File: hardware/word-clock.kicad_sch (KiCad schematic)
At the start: 51 parts, among them SW1 Hour, SW2 Minute, SW3 Audio, U1 ESP32 CP2102, U2 74HC245

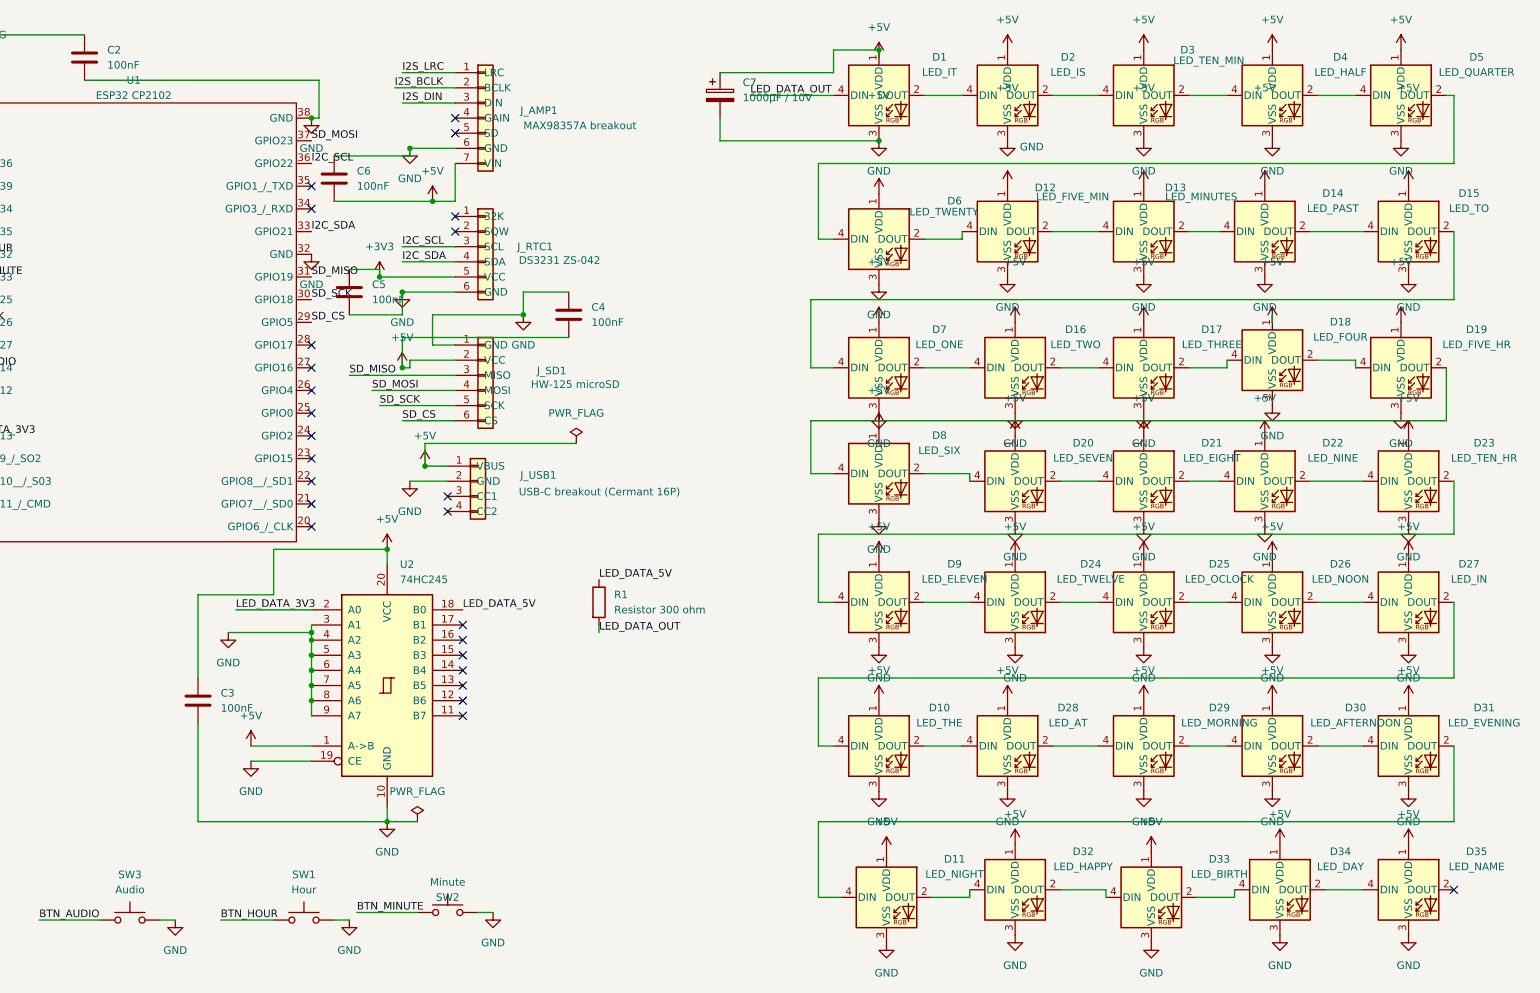
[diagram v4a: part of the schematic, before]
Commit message: feat(hardware): led chain reorder, AT relocated, routing + pour complete
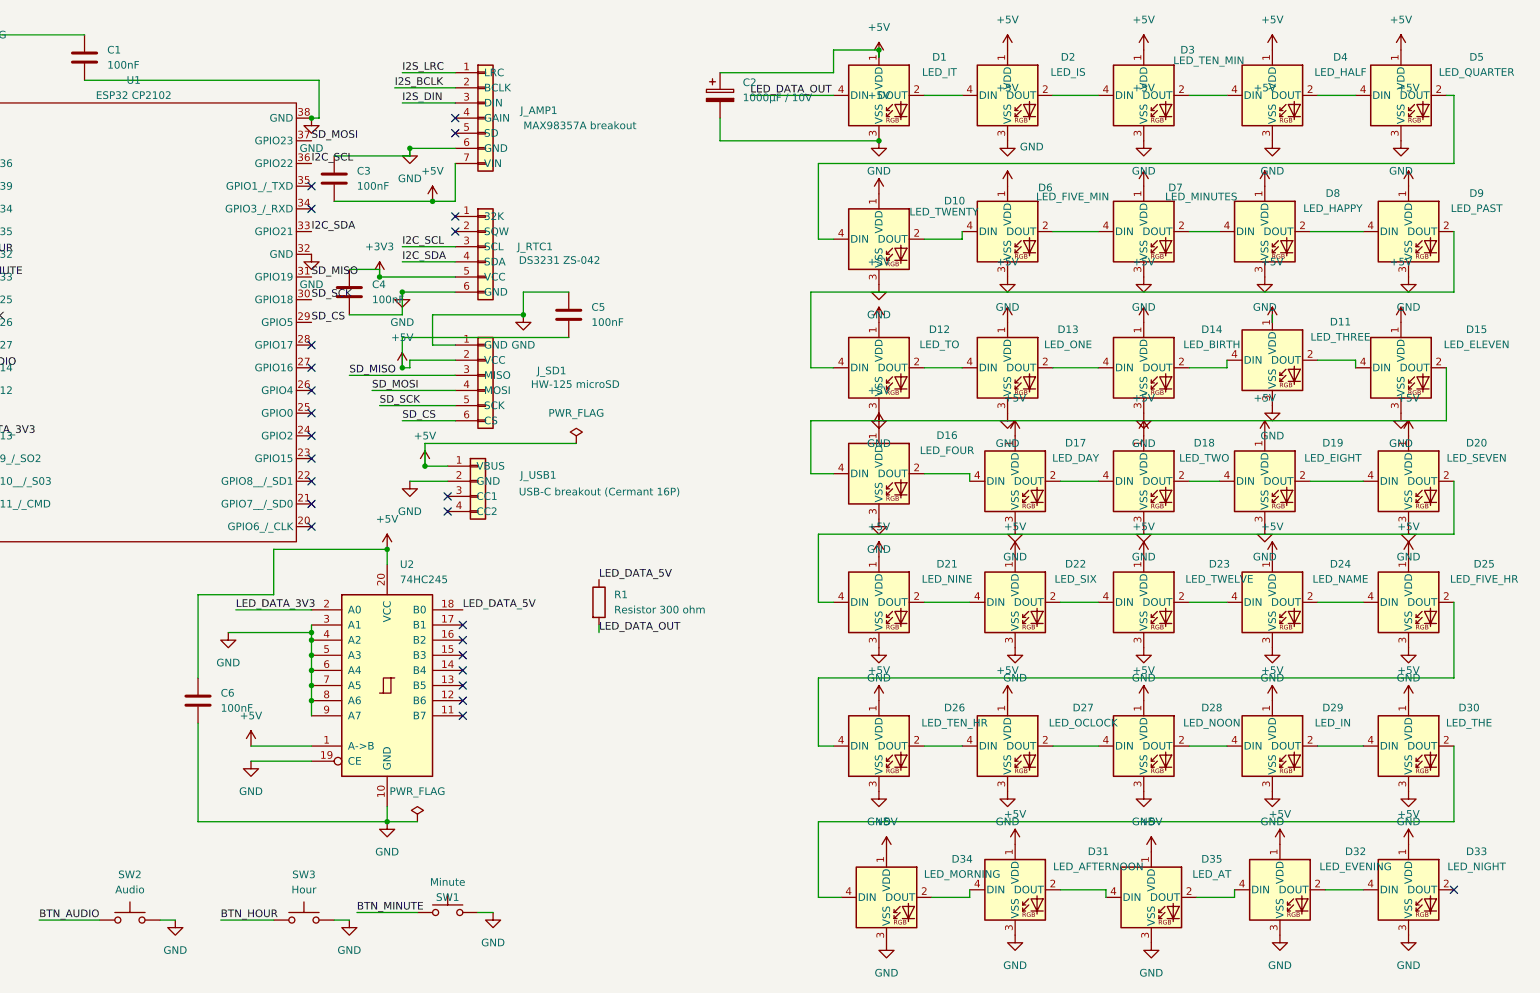
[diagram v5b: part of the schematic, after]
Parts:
- renumbered C2 to C1, C7 to C2, C6 to C3, C5 to C4, C4 to C5, C3 to C6, D6 to D10, D17 to D11, D15 to D12, D7 to D13, D33 to D14, D9 to D15, D18 to D16, D34 to D17, D16 to D18, D21 to D19, D22 to D21, D8 to D22, D24 to D23, D35 to D24, D19 to D25, D23 to D26, D25 to D27, D26 to D28, D27 to D29, D10 to D30, D30 to D31, D31 to D32, D11 to D33, D29 to D34, D28 to D35, D12 to D6, D13 to D7, D32 to D8, D14 to D9, SW2 to SW1, SW3 to SW2, SW1 to SW3
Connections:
- net at D25.2 (DOUT): now also D26.4 (DIN); no longer D22.4 (DIN)
- net at D25.4 (DIN): now also D24.2 (DOUT); no longer D16.2 (DOUT)
- net at D7.2 (DOUT): now also D8.4 (DIN); no longer D9.4 (DIN)
- net at D23.2 (DOUT): now also D24.4 (DIN); no longer D27.4 (DIN)
- net at D23.4 (DIN): now also D22.2 (DOUT); no longer D15.2 (DOUT)
- net at D11.2 (DOUT): now also D15.4 (DIN); no longer D16.4 (DIN)
- net at D11.4 (DIN): now also D14.2 (DOUT); no longer D18.2 (DOUT)
- net at D17.2 (DOUT): now also D18.4 (DIN); no longer D24.4 (DIN)
- net at D17.4 (DIN): now also D16.2 (DOUT); no longer D14.2 (DOUT)
- net at D31.2 (DOUT): now also D35.4 (DIN); no longer D32.4 (DIN)
- net at D33.2 (DOUT): no longer D8.4 (DIN)
- net at D26.2 (DOUT): now also D27.4 (DIN); no longer D15.4 (DIN)
- net at D21.2 (DOUT): now also D22.4 (DIN); no longer D26.4 (DIN)
- net at D30.2 (DOUT): now also D34.4 (DIN); no longer D35.4 (DIN)
- net at D21.4 (DIN): now also D20.2 (DOUT); no longer D19.2 (DOUT)
- net at D35.2 (DOUT): now also D32.4 (DIN); no longer D34.4 (DIN)
- net at D19.4 (DIN): now also D18.2 (DOUT); no longer D20.2 (DOUT)
- net at D20.4 (DIN): now also D19.2 (DOUT); no longer D22.2 (DOUT)
- net at D13.2 (DOUT): now also D14.4 (DIN); no longer D18.4 (DIN)
- net at D8.2 (DOUT): now also D9.4 (DIN); no longer D14.4 (DIN)
- new net: D15.2 (DOUT), D16.4 (DIN)
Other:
- moved on the sheet: D11, D12, D13, D14, D15, D16, D17, D18, D19, D20, D21, D22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

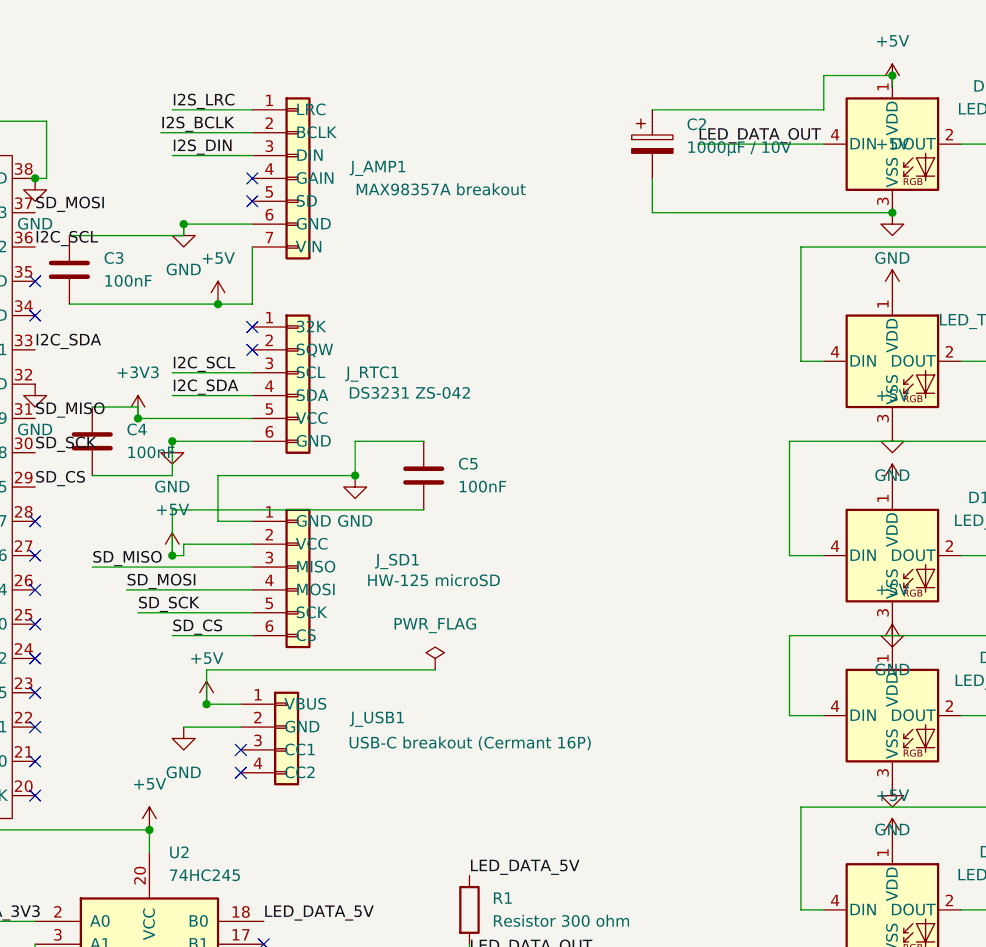
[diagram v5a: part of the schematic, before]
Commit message: fix(hardware): remove cermant usb-c breakout, power via esp32 micro-usb
Removes J_USB1 from the schematic and PCB. The user-facing USB-C port on
the back panel will now be provided by a panel-mount USB-C-female-to-
micro-USB-male pigtail plugged directly into the ESP32 module's native
micro-USB connector. The CP2102 bridge on the module handles both power
and firmware flashing — one port, one hole in the back panel, no PCB
data-routing rework needed.

PWR_FLAG on +5V re-attached to the module's 5V pin to satisfy ERC.

Downstream docs updated:
- pinout.md Power/Input line now describes the new path.
- phase-2-parts-list.md marks the old USB-C breakout as superseded on the
  final PCB (still useful for breadboard bring-up) and adds the panel-
  mount pigtail as its own line item.

Open: when the AITRIP ESP32 modules arrive, inspect the micro-USB input
for a polyfuse. If a 500 mA fuse is present it will nuisance-trip under
LEDs + audio — bridge or replace before fab.
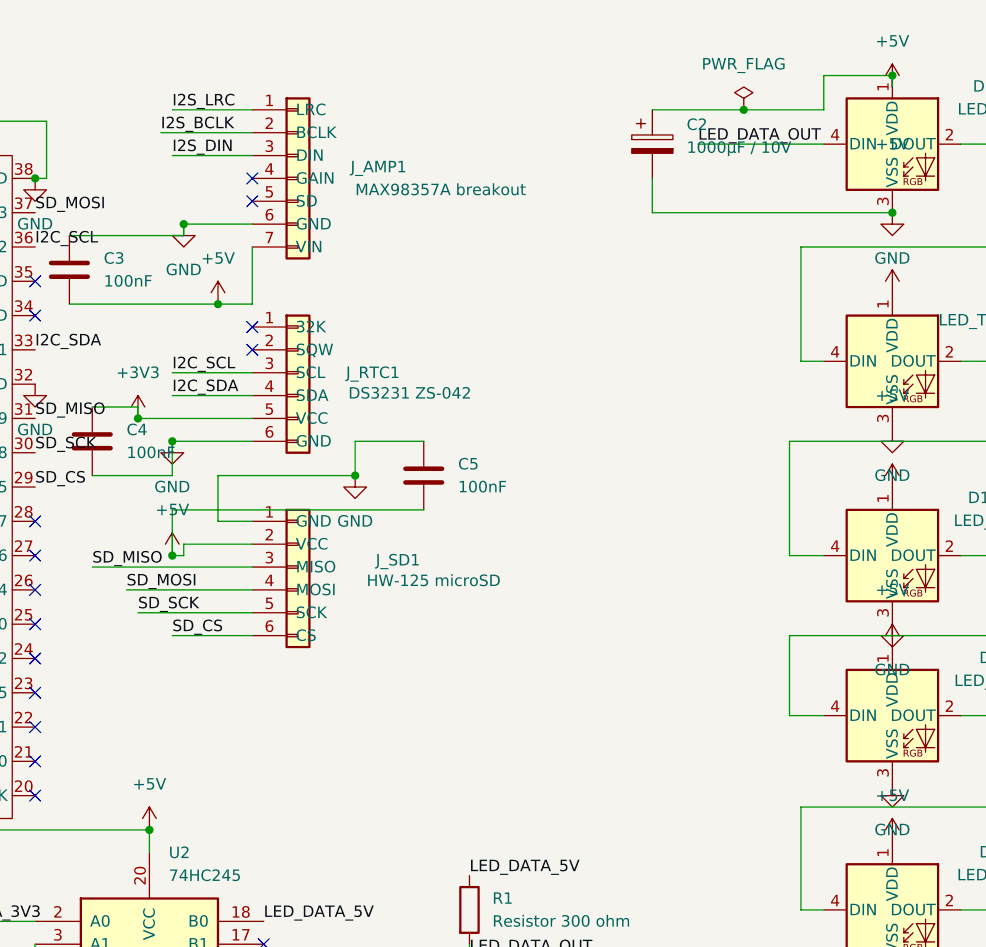
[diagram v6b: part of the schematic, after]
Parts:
- removed J_USB1: USB-C breakout (Cermant 16P), Connector_PinHeader_2.54mm:PinHeader_1x16_P2.54mm_Vertical, symbol Connector_Generic:Conn_01x04
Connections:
- no-connect marks 34 -> 32

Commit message: fix(hardware): swap J_RTC1 and J_SD1 to right-angle female sockets
DS3231 (HW-084) and HW-125 modules ship with right-angle pins that
don't fit into vertical through-hole sockets without bending. Swap the
PCB footprints from PinHeader_1x06_P2.54mm_Vertical to
PinSocket_1x06_P2.54mm_Horizontal so the daughterboards plug directly
in with the modules lying parallel to the main PCB.

Pad global positions preserved in both footprints so existing routing
is unchanged. J_SD1 keeps rot=180 with Y-mirrored coords (body extends
east into clear space); J_RTC1 uses rot=0 with un-mirrored coords
(body extends west, away from ESP32 at +X).

Also gitignore *.xlsx and word-clock-gerbers-*.zip so generated PCBA
artifacts don't pollute the repo (consistent with existing .gbr/.csv
rules).
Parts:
- J_RTC1, J_SD1: footprint Connector_PinHeader_2.54mm:PinHeader_1x06_P2.54mm_Vertical -> Connector_PinSocket_2.54mm:PinSocket_1x06_P2.54mm_Horizontal
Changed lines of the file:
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@@
 			)
 		)
-		(property "Footprint" "Connector_PinHeader_2.54mm:PinHeader_1x06_P2.54mm_Vertical"
+		(property "Footprint" "Connector_PinSocket_2.54mm:PinSocket_1x06_P2.54mm_Horizontal"
 			(at 104.14 69.85 0)
 			(hide yes)
@@
 			)
 		)
-		(property "Footprint" "Connector_PinHeader_2.54mm:PinHeader_1x06_P2.54mm_Vertical"
+		(property "Footprint" "Connector_PinSocket_2.54mm:PinSocket_1x06_P2.54mm_Horizontal"
 			(at 104.14 48.26 0)
 			(hide yes)

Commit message: feat(hardware): commit as-fabricated 63-LED board
The 63-LED board ordered from JLCPCB 2026-06-07 lived only in the working
tree and an untracked fab zip; the last hardware commit was the
superseded 35-LED April design. Commit the canonical KiCad source, the
custom daughtercard footprints (word-clock.pretty/ + fp-lib-table), and
the exact as-ordered fab package so the design that became the physical
clocks is under version control for the 40-year horizon.

Also add the pre-fab review and caliper-measured daughtercard dimensions,
and record the B.Cu +5V / F.Cu GND power-plane split in CLAUDE.md.
hardware/fab/README.md notes the WS2812B-B/W -> WS2812B-V6 (C52917433)
as-built LED substitution so the archived BOM is not misleading.
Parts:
- removed D7: LED_MINUTES, LED_SMD:LED_WS2812B_PLCC4_5.0x5.0mm_P3.2mm, symbol LED:WS2812B
- added C10, C11, C12, C13, C14, C15, C16, C17, C18, C19, C20, C21, C22, C23, C7, C8, C9: 100nF, Capacitor_THT:C_Disc_D5.0mm_W2.5mm_P5.00mm, symbol Device:C
- added D36: LED_HALF_1, LED_SMD:LED_WS2812B_PLCC4_5.0x5.0mm_P3.2mm, symbol LED:WS2812B
- added D37: LED_QUARTER_1, LED_SMD:LED_WS2812B_PLCC4_5.0x5.0mm_P3.2mm, symbol LED:WS2812B
- added D38: LED_QUARTER_2, LED_SMD:LED_WS2812B_PLCC4_5.0x5.0mm_P3.2mm, symbol LED:WS2812B
- added D39: LED_TWENTY_1, LED_SMD:LED_WS2812B_PLCC4_5.0x5.0mm_P3.2mm, symbol LED:WS2812B
- added D40: LED_FIVE_MIN_1, LED_SMD:LED_WS2812B_PLCC4_5.0x5.0mm_P3.2mm, symbol LED:WS2812B
- added D41: LED_MINUTES_1, LED_SMD:LED_WS2812B_PLCC4_5.0x5.0mm_P3.2mm, symbol LED:WS2812B
- added D42: LED_MINUTES_2, LED_SMD:LED_WS2812B_PLCC4_5.0x5.0mm_P3.2mm, symbol LED:WS2812B
- added D43: LED_HAPPY_1, LED_SMD:LED_WS2812B_PLCC4_5.0x5.0mm_P3.2mm, symbol LED:WS2812B
- added D44: LED_PAST_1, LED_SMD:LED_WS2812B_PLCC4_5.0x5.0mm_P3.2mm, symbol LED:WS2812B
- added D45: LED_BIRTH_1, LED_SMD:LED_WS2812B_PLCC4_5.0x5.0mm_P3.2mm, symbol LED:WS2812B
- added D46: LED_THREE_1, LED_SMD:LED_WS2812B_PLCC4_5.0x5.0mm_P3.2mm, symbol LED:WS2812B
- added D47: LED_ELEVEN_1, LED_SMD:LED_WS2812B_PLCC4_5.0x5.0mm_P3.2mm, symbol LED:WS2812B
- added D48: LED_FOUR_1, LED_SMD:LED_WS2812B_PLCC4_5.0x5.0mm_P3.2mm, symbol LED:WS2812B
- added D49: LED_EIGHT_1, LED_SMD:LED_WS2812B_PLCC4_5.0x5.0mm_P3.2mm, symbol LED:WS2812B
- added D50: LED_SEVEN_1, LED_SMD:LED_WS2812B_PLCC4_5.0x5.0mm_P3.2mm, symbol LED:WS2812B
- added D51: LED_NINE_1, LED_SMD:LED_WS2812B_PLCC4_5.0x5.0mm_P3.2mm, symbol LED:WS2812B
- added D52: LED_TWELVE_1, LED_SMD:LED_WS2812B_PLCC4_5.0x5.0mm_P3.2mm, symbol LED:WS2812B
- added D53: LED_NAME_1, LED_SMD:LED_WS2812B_PLCC4_5.0x5.0mm_P3.2mm, symbol LED:WS2812B
- added D54: LED_FIVE_HR_1, LED_SMD:LED_WS2812B_PLCC4_5.0x5.0mm_P3.2mm, symbol LED:WS2812B
- added D55: LED_OCLOCK_1, LED_SMD:LED_WS2812B_PLCC4_5.0x5.0mm_P3.2mm, symbol LED:WS2812B
- added D56: LED_NOON_1, LED_SMD:LED_WS2812B_PLCC4_5.0x5.0mm_P3.2mm, symbol LED:WS2812B
- added D57: LED_MORNING_1, LED_SMD:LED_WS2812B_PLCC4_5.0x5.0mm_P3.2mm, symbol LED:WS2812B
- added D58: LED_MORNING_2, LED_SMD:LED_WS2812B_PLCC4_5.0x5.0mm_P3.2mm, symbol LED:WS2812B
- added D59: LED_AFTERNOON_2, LED_SMD:LED_WS2812B_PLCC4_5.0x5.0mm_P3.2mm, symbol LED:WS2812B
- added D60: LED_MINUTES, LED_SMD:LED_WS2812B_PLCC4_5.0x5.0mm_P3.2mm, symbol LED:WS2812B
- added D61: LED_EVENING_1, LED_SMD:LED_WS2812B_PLCC4_5.0x5.0mm_P3.2mm, symbol LED:WS2812B
- added D62: LED_EVENING_2, LED_SMD:LED_WS2812B_PLCC4_5.0x5.0mm_P3.2mm, symbol LED:WS2812B
- added D63: LED_NIGHT_1, LED_SMD:LED_WS2812B_PLCC4_5.0x5.0mm_P3.2mm, symbol LED:WS2812B
- added D64: LED_EVENING, LED_SMD:LED_WS2812B_PLCC4_5.0x5.0mm_P3.2mm, symbol LED:WS2812B
- D32: value LED_EVENING -> LED_AFTERNOON_1
- J_AMP1: footprint Connector_PinHeader_2.54mm:PinHeader_1x07_P2.54mm_Vertical -> word-clock:Daughtercard_AMP_MAX98357A
- J_RTC1: footprint Connector_PinSocket_2.54mm:PinSocket_1x06_P2.54mm_Horizontal -> word-clock:Daughtercard_RTC_DS3231
- J_SD1: footprint Connector_PinSocket_2.54mm:PinSocket_1x06_P2.54mm_Horizontal -> word-clock:Daughtercard_SD_HW125
- U2: value 74HC245 -> 74HCT245; symbol 74xx:74HC245 -> 74xx:74HCT245
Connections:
- net +3V3: no longer C1.1
- net +5V: now also C1.1, C10.1, C11.1, C12.1, C13.1, C14.1, C15.1, C16.1, C17.1, C18.1, C19.1, C20.1, C21.1, C22.1, C23.1, C7.1, C8.1, C9.1, D36.1 (VDD), D37.1 (VDD), D38.1 (VDD), D39.1 (VDD), D40.1 (VDD), D41.1 (VDD), D42.1 (VDD), D43.1 (VDD), D44.1 (VDD), D45.1 (VDD), D46.1 (VDD), D47.1 (VDD), D48.1 (VDD), D49.1 (VDD), D50.1 (VDD), D51.1 (VDD), D52.1 (VDD), D53.1 (VDD), D54.1 (VDD), D55.1 (VDD), D56.1 (VDD), D57.1 (VDD), D58.1 (VDD), D59.1 (VDD), D60.1 (VDD), D61.1 (VDD), D62.1 (VDD), D63.1 (VDD), D64.1 (VDD)
- net GND: now also C10.2, C11.2, C12.2, C13.2, C14.2, C15.2, C16.2, C17.2, C18.2, C19.2, C20.2, C21.2, C22.2, C23.2, C7.2, C8.2, C9.2, D36.3 (VSS), D37.3 (VSS), D38.3 (VSS), D39.3 (VSS), D40.3 (VSS), D41.3 (VSS), D42.3 (VSS), D43.3 (VSS), D44.3 (VSS), D45.3 (VSS), D46.3 (VSS), D47.3 (VSS), D48.3 (VSS), D49.3 (VSS), D50.3 (VSS), D51.3 (VSS), D52.3 (VSS), D53.3 (VSS), D54.3 (VSS), D55.3 (VSS), D56.3 (VSS), D57.3 (VSS), D58.3 (VSS), D59.3 (VSS), D60.3 (VSS), D61.3 (VSS), D62.3 (VSS), D63.3 (VSS), D64.3 (VSS)
- net at D25.2 (DOUT): now also D54.4 (DIN); no longer D26.4 (DIN)
- net at D25.4 (DIN): now also D53.2 (DOUT); no longer D24.2 (DOUT)
- net at D8.4 (DIN): now also D42.2 (DOUT)
- net at D6.2 (DOUT): now also D40.4 (DIN)
- net at D23.2 (DOUT): now also D52.4 (DIN); no longer D24.4 (DIN)
- net at D28.2 (DOUT): now also D56.4 (DIN); no longer D29.4 (DIN)
- net at D28.4 (DIN): now also D55.2 (DOUT); no longer D27.2 (DOUT)
- net at D6.4 (DIN): now also D39.2 (DOUT); no longer D10.2 (DOUT)
- net at D15.4 (DIN): now also D46.2 (DOUT); no longer D11.2 (DOUT)
- net at D11.4 (DIN): now also D45.2 (DOUT); no longer D14.2 (DOUT)
- net at D9.2 (DOUT): now also D44.4 (DIN); no longer D12.4 (DIN)
- net at D9.4 (DIN): now also D43.2 (DOUT); no longer D8.2 (DOUT)
- net at D17.4 (DIN): now also D48.2 (DOUT); no longer D16.2 (DOUT)
- net at D4.2 (DOUT): now also D36.4 (DIN); no longer D5.4 (DIN)
- net at D10.4 (DIN): now also D38.2 (DOUT); no longer D5.2 (DOUT)
- net at D31.2 (DOUT): now also D32.4 (DIN); no longer D35.4 (DIN)
- net at D34.2 (DOUT): now also D57.4 (DIN); no longer D31.4 (DIN)
- net at D33.2 (DOUT): now also D63.4 (DIN)
- net at D33.4 (DIN): now also D62.2 (DOUT); no longer D32.2 (DOUT)
- net at D22.4 (DIN): now also D51.2 (DOUT); no longer D21.2 (DOUT)
- net at D21.4 (DIN): now also D50.2 (DOUT); no longer D20.2 (DOUT)
- net at D20.4 (DIN): now also D49.2 (DOUT); no longer D19.2 (DOUT)
- net at D16.4 (DIN): now also D47.2 (DOUT); no longer D15.2 (DOUT)
- net at D35.2 (DOUT): now also D64.4 (DIN); no longer D32.4 (DIN)
- new net: D41.4 (DIN), D60.2 (DOUT)
- new net: D40.2 (DOUT), D60.4 (DIN)
- new net: D15.2 (DOUT), D47.4 (DIN)
- new net: D11.2 (DOUT), D46.4 (DIN)
- new net: D12.4 (DIN), D44.2 (DOUT)
- new net: D29.4 (DIN), D56.2 (DOUT)
- new net: D14.2 (DOUT), D45.4 (DIN)
- new net: D37.2 (DOUT), D38.4 (DIN)
- new net: D27.2 (DOUT), D55.4 (DIN)
- new net: D24.2 (DOUT), D53.4 (DIN)
- new net: D24.4 (DIN), D52.2 (DOUT)
- new net: D37.4 (DIN), D5.2 (DOUT)
- new net: D36.2 (DOUT), D5.4 (DIN)
- new net: D26.4 (DIN), D54.2 (DOUT)
- new net: D20.2 (DOUT), D50.4 (DIN)
- new net: D61.2 (DOUT), D62.4 (DIN)
- new net: D32.2 (DOUT), D59.4 (DIN)
- new net: D21.2 (DOUT), D51.4 (DIN)
- new net: D57.2 (DOUT), D58.4 (DIN)
- new net: D61.4 (DIN), D64.2 (DOUT)
- new net: D41.2 (DOUT), D42.4 (DIN)
- new net: D16.2 (DOUT), D48.4 (DIN)
- new net: D19.2 (DOUT), D49.4 (DIN)
- new net: D35.4 (DIN), D59.2 (DOUT)
- new net: D31.4 (DIN), D58.2 (DOUT)
- new net: D43.4 (DIN), D8.2 (DOUT)
- new net: D10.2 (DOUT), D39.4 (DIN)
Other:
- moved on the sheet: D10, D11, D12, D13, D14, D15, D16, D17, D18, D19, D20, D21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
